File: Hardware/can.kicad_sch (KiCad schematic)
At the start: 9 parts, among them U2 SN65HVD230

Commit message: 30V compatibility update
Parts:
- R8: footprint Resistor_SMD:R_0603_1608Metric -> Resistor_SMD:R_0402_1005Metric
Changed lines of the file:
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@@
 			)
 		)
-		(property "Footprint" "Resistor_SMD:R_0603_1608Metric"
+		(property "Footprint" "Resistor_SMD:R_0402_1005Metric"
 			(at 124.46 95.25 0)
 			(effects

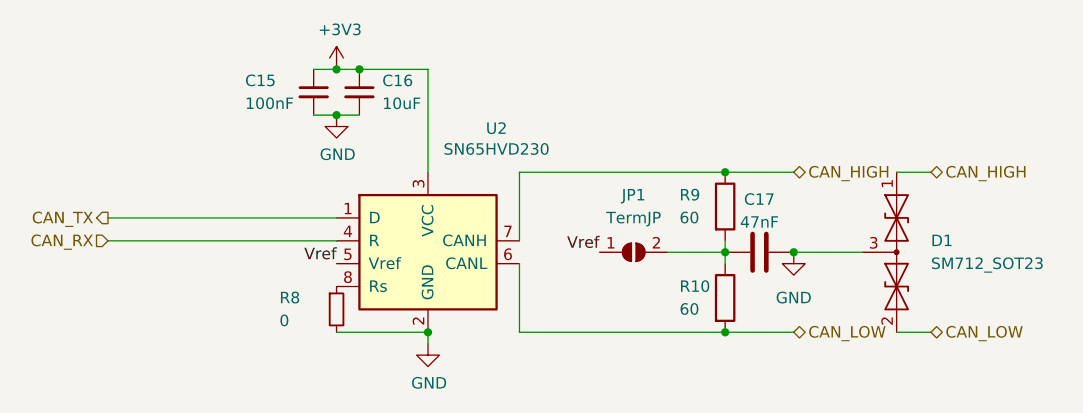
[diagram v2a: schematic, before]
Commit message: cleaned up schematic and bom
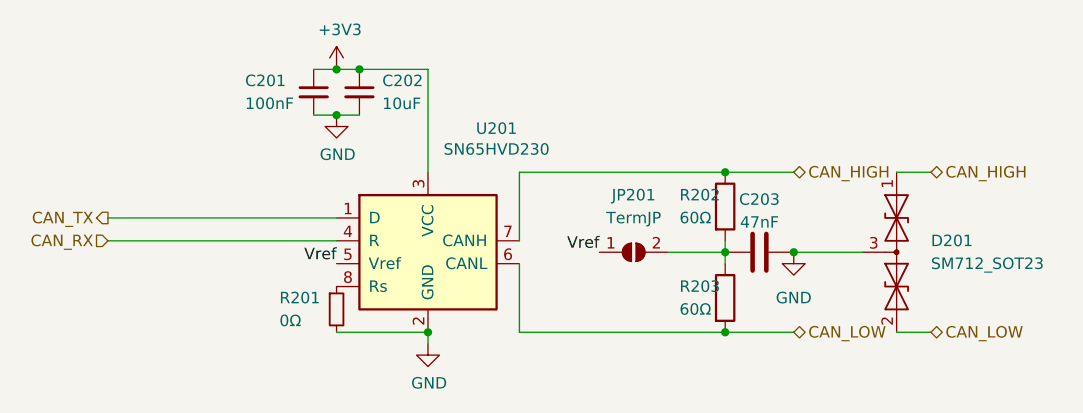
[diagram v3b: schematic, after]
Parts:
- JP201: renamed from JP1; now left out of the parts list
- R201: renamed from R8; value 0 -> 0Ω
- R202: renamed from R9; value 60 -> 60Ω
- R203: renamed from R10; value 60 -> 60Ω
- renumbered C15 to C201, C16 to C202, C17 to C203, D1 to D201, U2 to U201
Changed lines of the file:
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@@
 (kicad_sch
-	(version 20231120)
+	(version 20250114)
 	(generator "eeschema")
-	(generator_version "8.0")
+	(generator_version "9.0")
 	(paper "A4")
 	(junction
@@
 	(label "Vref"
 		(at 124.46 90.17 180)
-		(fields_autoplaced yes)
 		(effects
 			(font
@@
 	(label "Vref"
 		(at 153.67 88.9 180)
-		(fields_autoplaced yes)
 		(effects
 			(font
@@
 		(shape input)
 		(at 99.06 87.63 180)
-		(fields_autoplaced yes)
 		(effects
 			(font
@@
 		(shape bidirectional)
 		(at 175.26 80.01 0)
-		(fields_autoplaced yes)
 		(effects
 			(font
@@
 		(shape output)
 		(at 99.06 85.09 180)
-		(fields_autoplaced yes)
 		(effects
 			(font
@@
 		(shape bidirectional)
 		(at 190.5 80.01 0)
-		(fields_autoplaced yes)
 		(effects
 			(font
@@
 		(shape bidirectional)
 		(at 190.5 97.79 0)
-		(fields_autoplaced yes)
 		(effects
 			(font
@@
 		(shape bidirectional)
 		(at 175.26 97.79 0)
-		(fields_autoplaced yes)
 		(effects
 			(font
@@
 		(dnp no)
 		(fields_autoplaced yes)
-		(property "Reference" "#PWR032"
+		(property "Reference" "#PWR0203"
 			(at 134.62 105.41 0)
 			(effects
@@
 			(project "Chad"
 				(path "/7db990e4-92e1-4f99-b4d2-435bbec1ba83/00000000-0000-0000-0000-000061942b9a"
-					(reference "#PWR032")
+					(reference "#PWR0203")
 					(unit 1)
 				)
@@
 		(dnp no)
 		(fields_autoplaced yes)
-		(property "Reference" "#PWR030"
+		(property "Reference" "#PWR0201"
 			(at 124.46 72.39 0)
 			(effects
@@
 			(project "Chad"
 				(path "/7db990e4-92e1-4f99-b4d2-435bbec1ba83/00000000-0000-0000-0000-000061942b9a"
-					(reference "#PWR030")
+					(reference "#PWR0201")
 					(unit 1)
 				)
@@
 		(dnp no)
 		(fields_autoplaced yes)
-		(property "Reference" "U2"
+		(property "Reference" "U201"
 			(at 142.24 75.1586 0)
 			(effects
@@
 			(project "Chad"
 				(path "/7db990e4-92e1-4f99-b4d2-435bbec1ba83/00000000-0000-0000-0000-000061942b9a"
-					(reference "U2")
+					(reference "U201")
 					(unit 1)
 				)
@@
 		(dnp no)
 		(fields_autoplaced yes)
-		(property "Reference" "C16"
+		(property "Reference" "C202"
 			(at 129.54 69.8562 0)
 			(effects
@@
 			(project "Chad"
 				(path "/7db990e4-92e1-4f99-b4d2-435bbec1ba83/00000000-0000-0000-0000-000061942b9a"
-					(reference "C16")
+					(reference "C202")
 					(unit 1)
 				)
@@
 		(dnp no)
 		(fields_autoplaced yes)
-		(property "Reference" "D1"
+		(property "Reference" "D201"
 			(at 190.5 87.63 90)
 			(effects
@@
 			(project "Chad"
 				(path "/7db990e4-92e1-4f99-b4d2-435bbec1ba83/00000000-0000-0000-0000-000061942b9a"
-					(reference "D1")
+					(reference "D201")
 					(unit 1)
 				)
@@
 		(dnp no)
 		(fields_autoplaced yes)
-		(property "Reference" "#PWR033"
+		(property "Reference" "#PWR0204"
 			(at 175.26 95.25 0)
 			(effects
@@
 			(project "Chad"
 				(path "/7db990e4-92e1-4f99-b4d2-435bbec1ba83/00000000-0000-0000-0000-000061942b9a"
-					(reference "#PWR033")
+					(reference "#PWR0204")
 					(unit 1)
 				)
@@
 		(dnp no)
 		(fields_autoplaced yes)
-		(property "Reference" "C15"
+		(property "Reference" "C201"
 			(at 114.3 69.85 0)
 			(effects
@@
 			(project "Chad"
 				(path "/7db990e4-92e1-4f99-b4d2-435bbec1ba83/00000000-0000-0000-0000-000061942b9a"
-					(reference "C15")
+					(reference "C201")
 					(unit 1)
 				)
@@
 		(on_board yes)
 		(dnp no)
-		(property "Reference" "R8"
+		(property "Reference" "R201"
 			(at 118.11 93.98 0)
 			(effects
@@
 			)
 		)
-		(property "Value" "0"
+		(property "Value" "0Ω"
 			(at 118.11 96.52 0)
 			(effects
@@
 			(project "Chad"
 				(path "/7db990e4-92e1-4f99-b4d2-435bbec1ba83/00000000-0000-0000-0000-000061942b9a"
-					(reference "R8")
+					(reference "R201")
 					(unit 1)
 				)
@@
 		(dnp no)
 		(fields_autoplaced yes)
-		(property "Reference" "R10"
+		(property "Reference" "R203"
 			(at 162.56 92.71 0)
 			(effects
@@
 			)
 		)
-		(property "Value" "60"
+		(property "Value" "60Ω"
 			(at 162.56 95.25 0)
 			(effects
@@
 			(project "Chad"
 				(path "/7db990e4-92e1-4f99-b4d2-435bbec1ba83/00000000-0000-0000-0000-000061942b9a"
-					(reference "R10")
+					(reference "R203")
 					(unit 1)
 				)
@@
 		(dnp no)
 		(fields_autoplaced yes)
-		(property "Reference" "R9"
+		(property "Reference" "R202"
 			(at 162.56 82.55 0)
 			(effects
@@
 			)
 		)
-		(property "Value" "60"
+		(property "Value" "60Ω"
 			(at 162.56 85.09 0)
 			(effects
@@
 			(project "Chad"
 				(path "/7db990e4-92e1-4f99-b4d2-435bbec1ba83/00000000-0000-0000-0000-000061942b9a"
-					(reference "R9")
+					(reference "R202")
 					(unit 1)
 				)
@@
 		(dnp no)
 		(fields_autoplaced yes)
-		(property "Reference" "C17"
+		(property "Reference" "C203"
 			(at 171.45 83.0412 90)
 			(effects
@@
 			(project "Chad"
 				(path "/7db990e4-92e1-4f99-b4d2-435bbec1ba83/00000000-0000-0000-0000-000061942b9a"
-					(reference "C17")
+					(reference "C203")
 					(unit 1)
 				)
@@
 		(dnp no)
 		(fields_autoplaced yes)
-		(property "Reference" "#PWR031"
+		(property "Reference" "#PWR0202"
 			(at 124.46 80.01 0)
 			(effects
@@
 			(project "Chad"
 				(path "/7db990e4-92e1-4f99-b4d2-435bbec1ba83/00000000-0000-0000-0000-000061942b9a"
-					(reference "#PWR031")
+					(reference "#PWR0202")
 					(unit 1)
 				)
@@
 		(unit 1)
 		(exclude_from_sim no)
-		(in_bom yes)
+		(in_bom no)
 		(on_board yes)
 		(dnp no)
 		(fields_autoplaced yes)
-		(property "Reference" "JP1"
+		(property "Reference" "JP201"
 			(at 157.48 82.55 0)
 			(effects
@@
 			(project "Chad"
 				(path "/7db990e4-92e1-4f99-b4d2-435bbec1ba83/00000000-0000-0000-0000-000061942b9a"
-					(reference "JP1")
-					(unit 1)
-				)
+					(reference "JP201")
+					(unit 1)
+				)
